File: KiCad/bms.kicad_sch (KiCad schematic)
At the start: 29 parts, among them Q2 NMOS, Q3 NMOS, Q4 NMOS, Q5 NMOS, Q6 PMOS, U5 BQ25730RSN

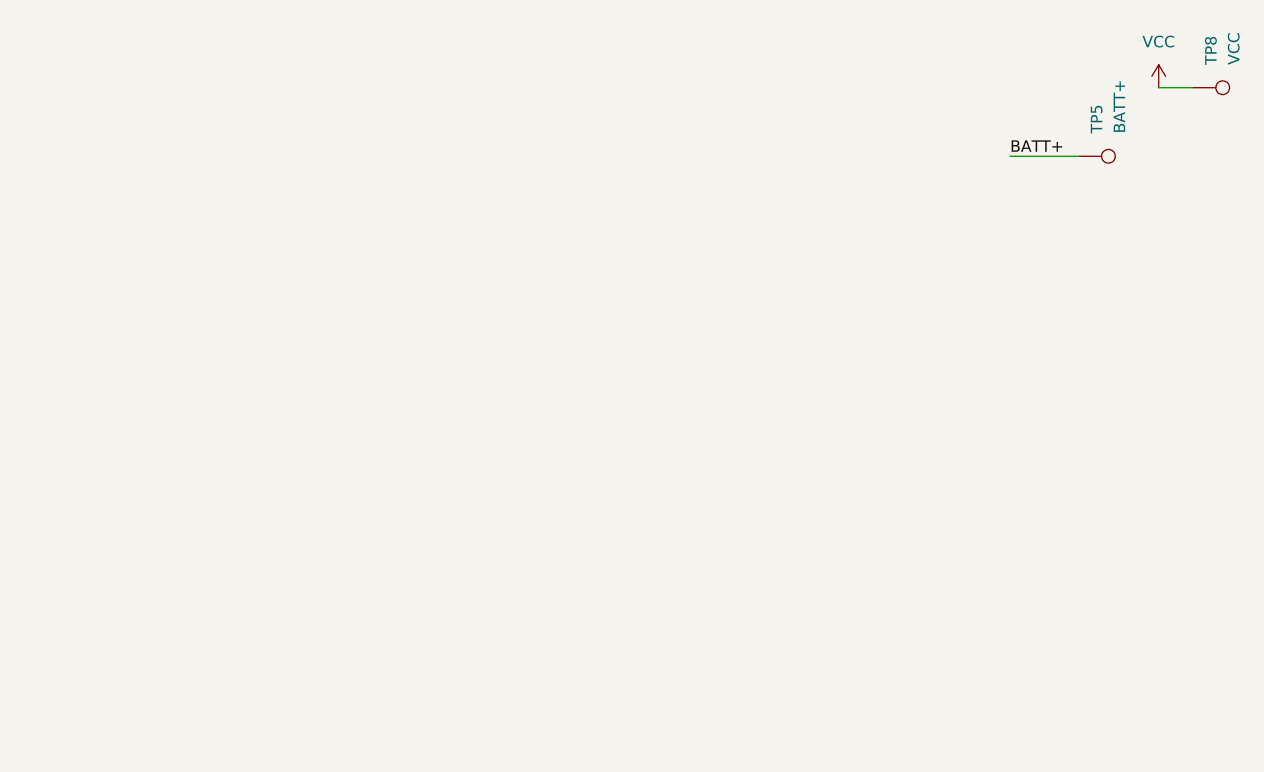
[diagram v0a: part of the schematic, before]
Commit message: Revert back to 1S configuration
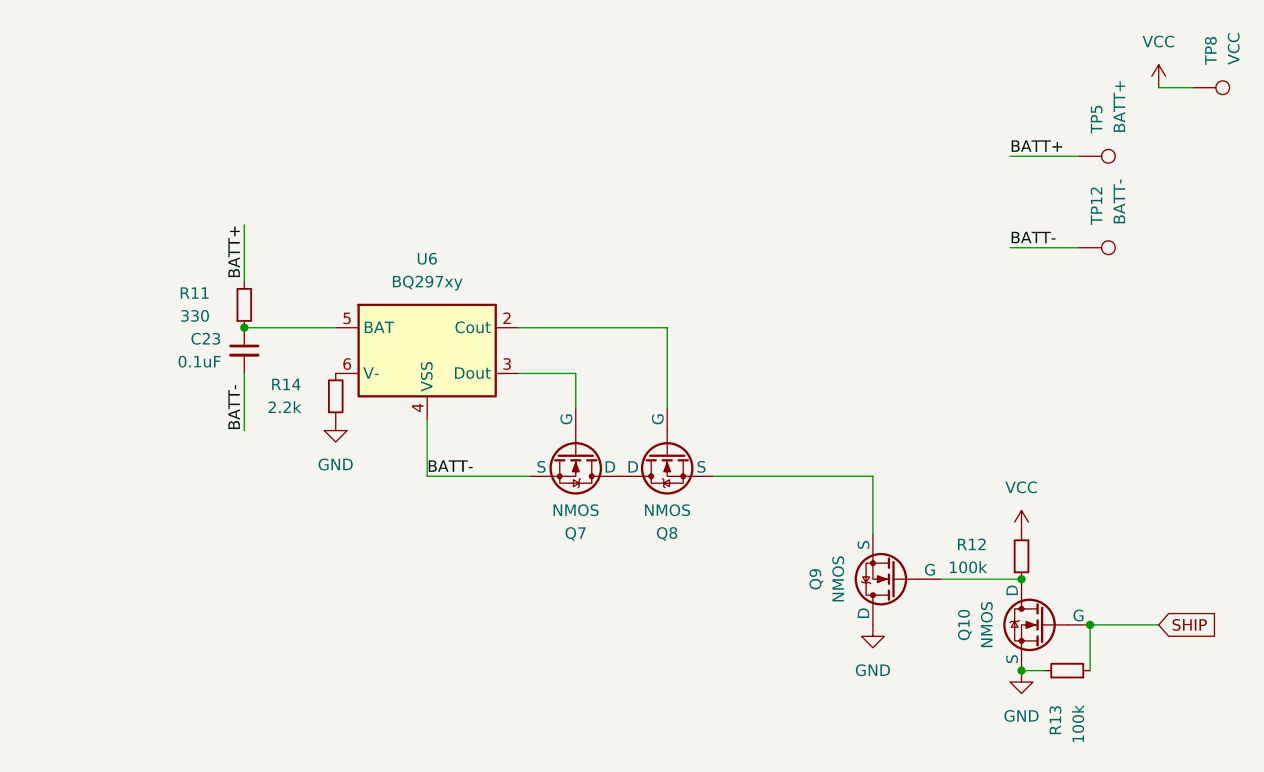
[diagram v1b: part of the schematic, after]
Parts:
- added C23: 0.1uF, Capacitor_SMD:C_0402_1005Metric, symbol Device:C_Small
- added Q10, Q7, Q8, Q9: NMOS, symbol Simulation_SPICE:NMOS
- added R11: 330, Resistor_SMD:R_0402_1005Metric, symbol Device:R_Small
- added R12, R13: 100k, Resistor_SMD:R_0402_1005Metric, symbol Device:R_Small
- added R14: 2.2k, Resistor_SMD:R_0402_1005Metric, symbol Device:R_Small
- added TP12: BATT-, TestPoint:TestPoint_Plated_Hole_D2.0mm, symbol Connector:TestPoint
- added U6: BQ297xy, Package_SON:WSON-6_1.5x1.5mm_P0.5mm, symbol Battery_Management:BQ297xy
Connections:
- net BATT+: now also R11.2
- net GND: now also Q10.3 (S), Q9.1 (D), R13.2, R14.1
- net VCC: now also R12.2
- new net: R14.2, U6.6 (V-)
- new net: Q7.1 (D), Q8.1 (D)
- new net: Q7.2 (G), U6.3 (Dout)
- new net: C23.1, R11.1, U6.5 (BAT)
- new net: Q10.1 (D), Q9.2 (G), R12.1
- new net: Q8.2 (G), U6.2 (Cout)
- new net: Q8.3 (S), Q9.3 (S)
- new net BATT-: C23.2, Q7.3 (S), TP12.1, U6.4 (VSS)
- new net SHIP: Q10.2 (G), R13.1

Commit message: More misc work
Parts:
- added C24: 0.1uF, Capacitor_SMD:C_0402_1005Metric, symbol Device:C_Small
- added C25: 1uF, Capacitor_SMD:C_0402_1005Metric, symbol Device:C_Small
- added C26, C27: 10uF, Capacitor_SMD:C_0603_1608Metric, symbol Device:C_Small
- added Q12: BSZ060, Package_SO:Vishay_PowerPAK_1212-8_Single, symbol Transistor_FET:DMT6008LFG
- added R15: 5m, symbol Device:R_Shunt
- added R16, R17: 10, Resistor_SMD:R_0402_1005Metric, symbol Device:R_Small
- Q10, Q2, Q3, Q4, Q5, Q7, Q8, Q9: value NMOS -> DMT3006; footprint (none) -> Package_DFN_QFN:Diodes_UDFN2020-6_Type-F; Digikey (none) -> https://www.digikey.com.au/en/products/detail/diodes-incorp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
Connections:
- net BATT+: now also C26.1, C27.1, R15.4
- net BATT-: now also Q7.4 (S), Q7.8 (S); no longer Q7.3 (S)
- net GND: now also Q10.4 (S), Q10.8 (S), Q3.4 (S), Q3.8 (S), Q4.4 (S), Q4.8 (S), Q9.2 (D), Q9.5 (D), Q9.6 (D), Q9.7 (D), C25.2, C26.2, C27.2; no longer Q10.3 (S), Q3.3 (S), Q4.3 (S)
- net HIDRV1: now also Q2.3 (G); no longer Q2.2 (G)
- net HIDRV2: now also Q5.3 (G); no longer Q5.2 (G)
- net LODRV1: now also Q3.3 (G); no longer Q3.2 (G)
- net LODRV2: now also Q4.3 (G); no longer Q4.2 (G)
- net SHIP: now also Q10.3 (G); no longer Q10.2 (G)
- net SRN: now also R17.1
- net SRP: now also R16.1
- net SW1: now also Q2.4 (S), Q2.8 (S), Q3.2 (D), Q3.5 (D), Q3.6 (D), Q3.7 (D); no longer Q2.3 (S)
- net SW2: now also Q4.2 (D), Q4.5 (D), Q4.6 (D), Q4.7 (D), Q5.4 (S), Q5.8 (S); no longer Q5.3 (S)
- net VCC: now also Q5.2 (D), Q5.5 (D), Q5.6 (D), Q5.7 (D)
- net at C16.1, C20.1, Q2.1 (D)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: now also Q2.2 (D), Q2.5 (D), Q2.6 (D), Q2.7 (D)
- net at Q6.1 (D): now also R15.1
- net at Q7.1 (D), Q8.1 (D): now also Q7.2 (D), Q7.5 (D), Q7.6 (D), Q7.7 (D), Q8.2 (D), Q8.5 (D), Q8.6 (D), Q8.7 (D)
- net at U6.3 (Dout): now also Q7.3 (G); no longer Q7.2 (G)
- net at Q10.1 (D), R12.1: now also Q10.2 (D), Q10.5 (D), Q10.6 (D), Q10.7 (D), Q9.3 (G); no longer Q9.2 (G)
- net at U6.2 (Cout): now also Q8.3 (G); no longer Q8.2 (G)
- new net: C24.1, C25.1, R15.2, R16.2
- new net: C24.2, R15.3, R17.2
- new net: Q8.4 (S), Q8.8 (S), Q9.4 (S), Q9.8 (S)
- new net: Q12.1 (S), Q12.2 (S), Q12.3 (S)
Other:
- moved on the sheet: C23, R11, R12, R13, R14, TP12, TP5, TP8, U6

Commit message: misc
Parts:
- removed R15: 5m, symbol Device:R_Shunt
- added C28: 3.3uF, Capacitor_SMD:C_0402_1005Metric, symbol Device:C_Small
- added C29: 1uF, Capacitor_SMD:C_0402_1005Metric, symbol Device:C_Small
- added C30, C31: 100pF, Capacitor_SMD:C_0402_1005Metric, symbol Device:C_Small
- added R15: 10m, Resistor_SMD:R_1206_3216Metric_Pad1.30x1.75mm_HandSolder, symbol Device:R
- added R18: 10, Resistor_SMD:R_0402_1005Metric, symbol Device:R_Small
- added R19: 380k, Resistor_SMD:R_0402_1005Metric, symbol Device:R_Small
- added R20: 220k, Resistor_SMD:R_0402_1005Metric, symbol Device:R_Small
- added R21: 191k, Resistor_SMD:R_0402_1005Metric, symbol Device:R_Small
- added R22: 30k, Resistor_SMD:R_0402_1005Metric, symbol Device:R_Small
- Q6: value PMOS -> DMP1009; footprint (none) -> Package_DFN_QFN:Diodes_UDFN2020-6_Type-F; Digikey (none) -> https://www.digikey.com.au/en/products/detail/diodes-incorp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
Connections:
- net BATT+: now also C24.2, R17.2, R15.2
- net GND: now also C28.2, C29.2, C30.2, C31.2, R20.1, R21.1, R22.1; no longer R14.1
- net VCC: now also Q6.4 (S), Q6.8 (S); no longer Q6.3 (S)
- net ~{BATDRV}: now also Q6.3 (G); no longer Q6.2 (G)
- net at Q6.1 (D): now also C24.1, C25.1, Q6.2 (D), Q6.5 (D), Q6.6 (D), Q6.7 (D), R16.2, R15.1
- net at U5.10 (PSYS): now also R22.2
- net REGN: now reaches U5.28 (REGN)
- net REGN: now also C28.1, R18.2
- net ILIM: now reaches U5.6 (ILIM)
- net ILIM: now also R19.1, R20.2
- net VDDA: now reaches U5.7 (VDDA)
- net VDDA: now also C29.1, R18.1, R19.2
- net at U5.8 (IADPT): now also C31.1, R21.2
- net at U5.9 (IBAT): now also C30.1
- net BATT-_2: now reaches Q8.4 (S), Q8.8 (S), Q9.4 (S), Q9.8 (S)
- net BATT-_2: now also R14.1

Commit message: More work for BMS portion
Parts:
- added C32: 33pF, Capacitor_SMD:C_0402_1005Metric, symbol Device:C_Small
- added C33: 4.7nF, Capacitor_SMD:C_0402_1005Metric, symbol Device:C_Small
- added C34: 15pF, Capacitor_SMD:C_0402_1005Metric, symbol Device:C_Small
- added C35: 680pF, Capacitor_SMD:C_0402_1005Metric, symbol Device:C_Small
- added R23: 40.2k, Resistor_SMD:R_0402_1005Metric, symbol Device:R_Small
- added R24: 15k, Resistor_SMD:R_0402_1005Metric, symbol Device:R_Small
- added R25: 750k, Resistor_SMD:R_0402_1005Metric, symbol Device:R_Small
- added R26: 250k, Resistor_SMD:R_0402_1005Metric, symbol Device:R_Small
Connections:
- net GND: now also C32.2, C33.2, C34.2, C35.2, R26.1
- net VDDA: now also R25.2
- net COMP1: now reaches U5.16 (COMP1)
- net COMP1: now also C34.1, R24.2
- net COMP2: now reaches U5.17 (COMP2)
- net COMP2: now also C32.1, R23.2
- net CELL_BATPRES: now reaches U5.18 (CELL_BATPRES)
- net CELL_BATPRES: now also R25.1, R26.2
- new net: C35.1, R24.1
- new net: C33.1, R23.1

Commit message: Move to using 100W-Charging-PCB for battery charge
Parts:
- removed C10, C15, C26, C27, C9: 10uF, Capacitor_SMD:C_0603_1608Metric, symbol Device:C_Small
- removed C11, C19: 100uF, Capacitor_Tantalum_SMD:CP_EIA-3216-10_Kemet-I, symbol Device:C_Polarized_Small
- removed C12, C13: 47nF, Capacitor_SMD:C_0402_1005Metric, symbol Device:C_Small
- removed C14, C16: 10nF, Capacitor_SMD:C_0402_1005Metric, symbol Device:C_Small
- removed C17, C18: 22uF, Capacitor_SMD:C_0402_1005Metric, symbol Device:C_Small
- removed C20: 1nF, Capacitor_SMD:C_0402_1005Metric, symbol Device:C_Small
- removed C21, C22: 33nF, Capacitor_SMD:C_0402_1005Metric, symbol Device:C_Small
- removed C23, C24: 0.1uF, Capacitor_SMD:C_0402_1005Metric, symbol Device:C_Small
- removed C25, C29, C8: 1uF, Capacitor_SMD:C_0402_1005Metric, symbol Device:C_Small
- removed C28: 3.3uF, Capacitor_SMD:C_0402_1005Metric, symbol Device:C_Small
- removed C30, C31: 100pF, Capacitor_SMD:C_0402_1005Metric, symbol Device:C_Small
- removed C32: 33pF, Capacitor_SMD:C_0402_1005Metric, symbol Device:C_Small
- removed C33: 4.7nF, Capacitor_SMD:C_0402_1005Metric, symbol Device:C_Small
- removed C34: 15pF, Capacitor_SMD:C_0402_1005Metric, symbol Device:C_Small
- removed C35: 680pF, Capacitor_SMD:C_0402_1005Metric, symbol Device:C_Small
- removed L1: 4.7uH, Inductor_SMD:L_APV_APH0420, symbol Device:L_Small
- removed Q10, Q2, Q3, Q4, Q5, Q7, Q8, Q9: DMT3006, Package_DFN_QFN:Diodes_UDFN2020-6_Type-F, symbol Simulation_SPICE:NMOS
- removed Q12: BSZ060, Package_SO:Vishay_PowerPAK_1212-8_Single, symbol Transistor_FET:DMT6008LFG
- removed Q6: DMP1009, Package_DFN_QFN:Diodes_UDFN2020-6_Type-F, symbol Simulation_SPICE:PMOS
- removed R10: 5m, Resistor_SMD:R_0805_2012Metric, symbol Device:R_Small
- removed R11: 330, Resistor_SMD:R_0402_1005Metric, symbol Device:R_Small
- removed R12, R13: 100k, Resistor_SMD:R_0402_1005Metric, symbol Device:R_Small
- removed R14: 2.2k, Resistor_SMD:R_0402_1005Metric, symbol Device:R_Small
- removed R15: 10m, Resistor_SMD:R_1206_3216Metric_Pad1.30x1.75mm_HandSolder, symbol Device:R
- removed R16, R17, R18: 10, Resistor_SMD:R_0402_1005Metric, symbol Device:R_Small
- removed R19: 380k, Resistor_SMD:R_0402_1005Metric, symbol Device:R_Small
- removed R20: 220k, Resistor_SMD:R_0402_1005Metric, symbol Device:R_Small
- removed R21: 191k, Resistor_SMD:R_0402_1005Metric, symbol Device:R_Small
- removed R22: 30k, Resistor_SMD:R_0402_1005Metric, symbol Device:R_Small
- removed R23: 40.2k, Resistor_SMD:R_0402_1005Metric, symbol Device:R_Small
- removed R24: 15k, Resistor_SMD:R_0402_1005Metric, symbol Device:R_Small
- removed R25: 750k, Resistor_SMD:R_0402_1005Metric, symbol Device:R_Small
- removed R26: 250k, Resistor_SMD:R_0402_1005Metric, symbol Device:R_Small
- removed R6: 2.2, Resistor_SMD:R_0402_1005Metric, symbol Device:R_Small
- removed R7, R8: 4.99, Resistor_SMD:R_0402_1005Metric, symbol Device:R_Small
- removed TP12: BATT-, TestPoint:TestPoint_Plated_Hole_D2.0mm, symbol Connector:TestPoint
- removed TP5: BATT+, TestPoint:TestPoint_Plated_Hole_D2.0mm, symbol Connector:TestPoint
- removed TP8: VCC, TestPoint:TestPoint_Plated_Hole_D2.0mm, symbol Connector:TestPoint
- removed TP9: GND, TestPoint:TestPoint_Plated_Hole_D2.0mm, symbol Connector:TestPoint
- removed U5: BQ25730RSN, Package_DFN_QFN:Texas_RSN_WQFN-32-1EP_4x4mm_P0.4mm_EP2.8x2.8mm_ThermalVias, symbol Battery_Management:BQ25895RTW
- removed U6: BQ297xy, Package_SON:WSON-6_1.5x1.5mm_P0.5mm, symbol Battery_Management:BQ297xy
